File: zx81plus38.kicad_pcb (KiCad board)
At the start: 2 copper layers, 142.2 x 99.1 mm, 131 parts, among them J1 LED on, J11 Expansion Header, J12 Expansion Header, J2 KB2, J3 KB1, Q1 2N3904, Q2 2N3904, Q3 2N3904, Q4 2N3904, Q5 2N3904, Q8 2N3904, Q9 2N3904, U1 74HC541, U10 74HC86, U11 74HC08, U12 74HC32, U13 74HC00, U14 74HC393, U15 74HC11, U16 74HC32, U18 74HC74, U19 74HC32, U2 Z80CPU, U21 74HC14, U22 74HC541, U23 74HC32, U24 74HC08, U27 74HC138, U28 74HC74, U29 74HC74, U3 KM62256CLP, U4 74HC574, U5 27C256, U6 74HC125, U7 74HC393, U8 74HC4002, U9 74HC165, Y1 13MHz

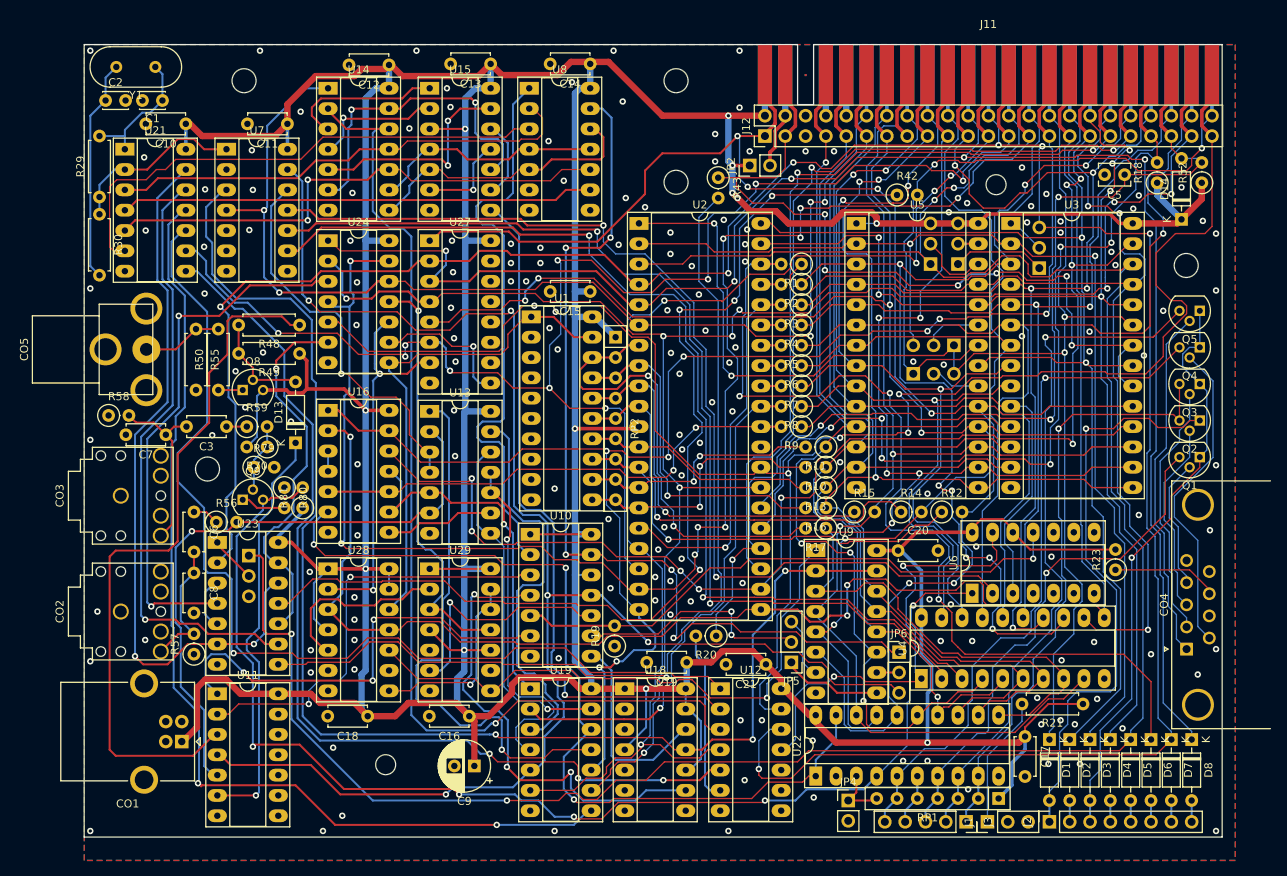
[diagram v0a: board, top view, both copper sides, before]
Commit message: fixed mounting hole positions
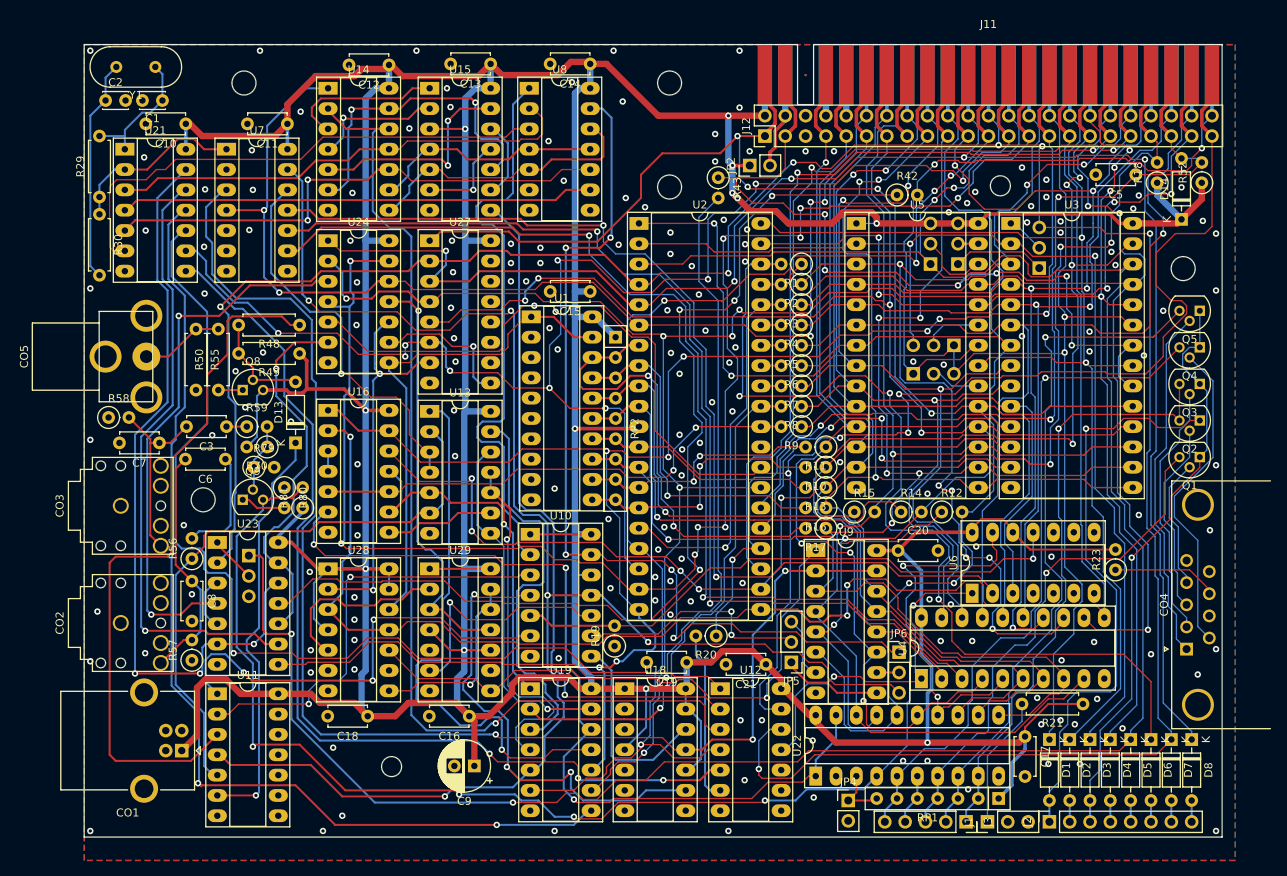
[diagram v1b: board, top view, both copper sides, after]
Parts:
- C5: footprint Capacitor_THT:C_Disc_D3.8mm_W2.6mm_P2.50mm -> Capacitor_THT:C_Disc_D4.7mm_W2.5mm_P5.00mm
- moved C6 7.69 mm to (76.1, 100.1), turned to 180 degrees
- moved R56 5.49 mm to (71.9, 112.5), turned to 90 degrees
- moved H7 3.89 mm to (73.3, 105.2)
- moved CO2 1.43 mm to (63.0, 120.6)
- moved C5 1.40 mm to (189.9, 64.5)
- moved C7 1.30 mm to (67.8, 98.0)
- moved CO3 1.26 mm to (63.0, 105.9)
- moved CO1 1.13 mm to (70.6, 136.5)
- moved C8 1.05 mm to (71.9, 115.3)
- moved H3 1.00 mm to (131.6, 66.1)
- moved CO5 0.90 mm to (61.1, 87.3)
- moved H2 0.86 mm to (131.6, 53.1)
- moved R57 0.80 mm to (71.9, 125.2)
- moved H6 0.78 mm to (96.8, 138.5)
- moved H5 0.56 mm to (172.9, 65.9)
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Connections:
- R56 pad 1: Net-(C6-Pad1) -> /nVSYNC
- R56 pad 2: /nVSYNC -> Net-(C6-Pad1)
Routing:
- net Net-(C6-Pad2): track 16.7 -> 29.9 mm
- net Net-(C6-Pad1): track 3.32 -> 14.0 mm
- net Net-(U21-Pad13): track 90.0 -> 94.0 mm, vias 2 -> 3
- net Net-(U12-Pad1): track 127.2 -> 128.7 mm
- net Net-(U23-Pad4): track 67.0 -> 68.5 mm
- net /A6': track 152.8 -> 151.5 mm
- net /nVSYNC: track 76.5 -> 75.3 mm, vias 1 -> 0
- net +5V: track 789.8 -> 791.0 mm
- net Net-(C3-Pad2): track 22.2 -> 23.2 mm
- net Net-(R48-Pad1): track 88.1 -> 89.0 mm
- net Net-(U21-Pad12): track 75.4 -> 76.2 mm
- net /nRESET: track 108.2 -> 107.5 mm
- net /A14: track 313.3 -> 312.8 mm
- net /A9: track 147.4 -> 146.9 mm
- net GND: vias 165 -> 169

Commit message: fixed keyboard connector
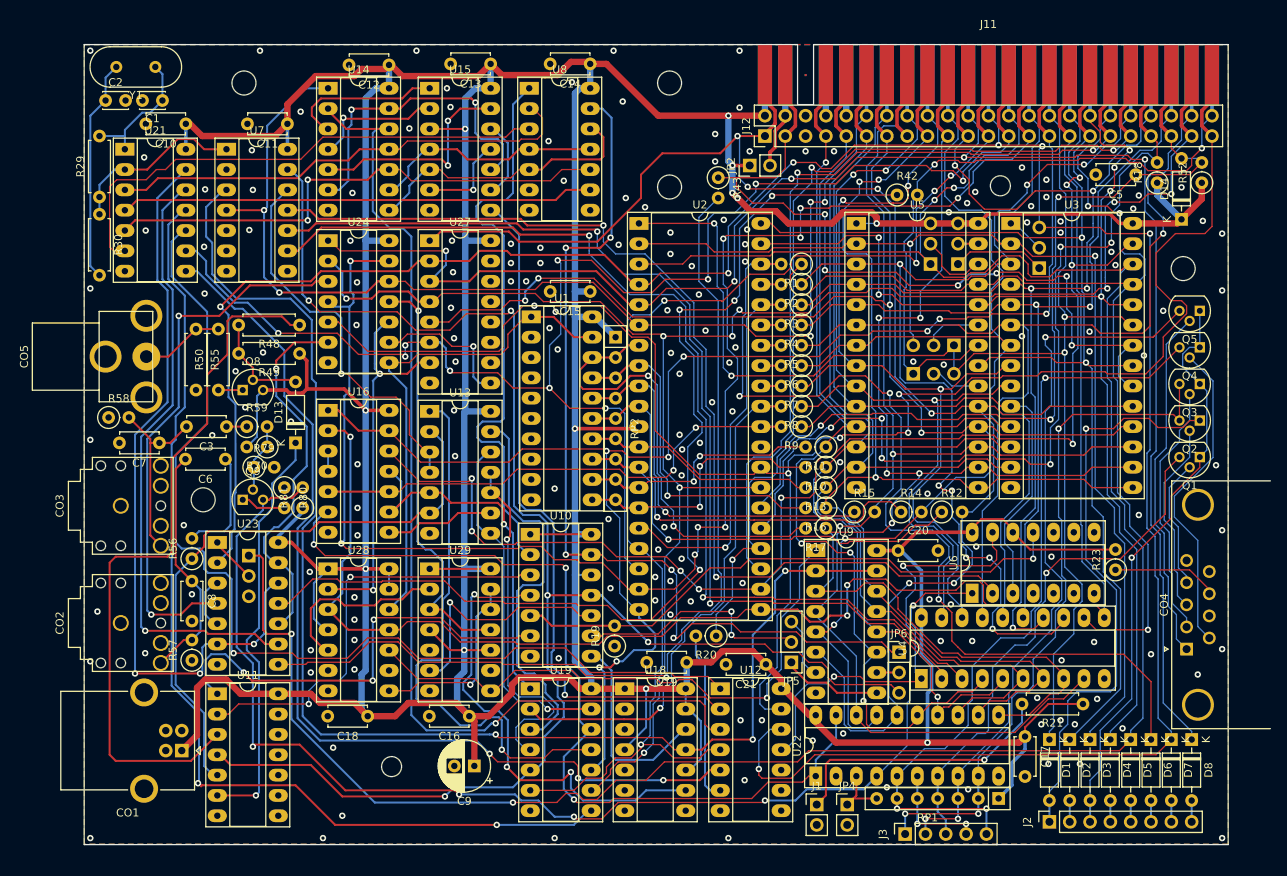
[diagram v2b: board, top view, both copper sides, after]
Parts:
- J1: footprint Connector_PinHeader_2.54mm:PinHeader_1x03_P2.54mm_Vertical -> Connector_PinHeader_2.54mm:PinHeader_1x02_P2.54mm_Vertical
- moved J1 21.4 mm to (150.0, 143.3), turned to 0 degrees
- moved J3 7.77 mm to (161.0, 146.9), turned to 90 degrees
- moved JP4 0.52 mm to (153.8, 143.3)
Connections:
- J1 pad 2: (no net) -> GND
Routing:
- net Net-(J1-Pad1): track 16.5 -> 34.5 mm, vias 0 -> 1
- net /KBD0: track 85.4 -> 97.4 mm, vias 1 -> 3
- net /KBD4: track 76.1 -> 86.1 mm, vias 1 -> 3
- net /KBD1: track 6.35 -> 13.3 mm, vias 0 -> 2
- net /KBD3: track 86.2 -> 91.2 mm, vias 1 -> 3
- net /KBD2: track 64.6 -> 65.9 mm
- net GND: vias 169 -> 168
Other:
- board size 142.2 x 99.1 mm -> 143 x 100 mm

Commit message: fixed CPU clock, memory decoder and video output latch
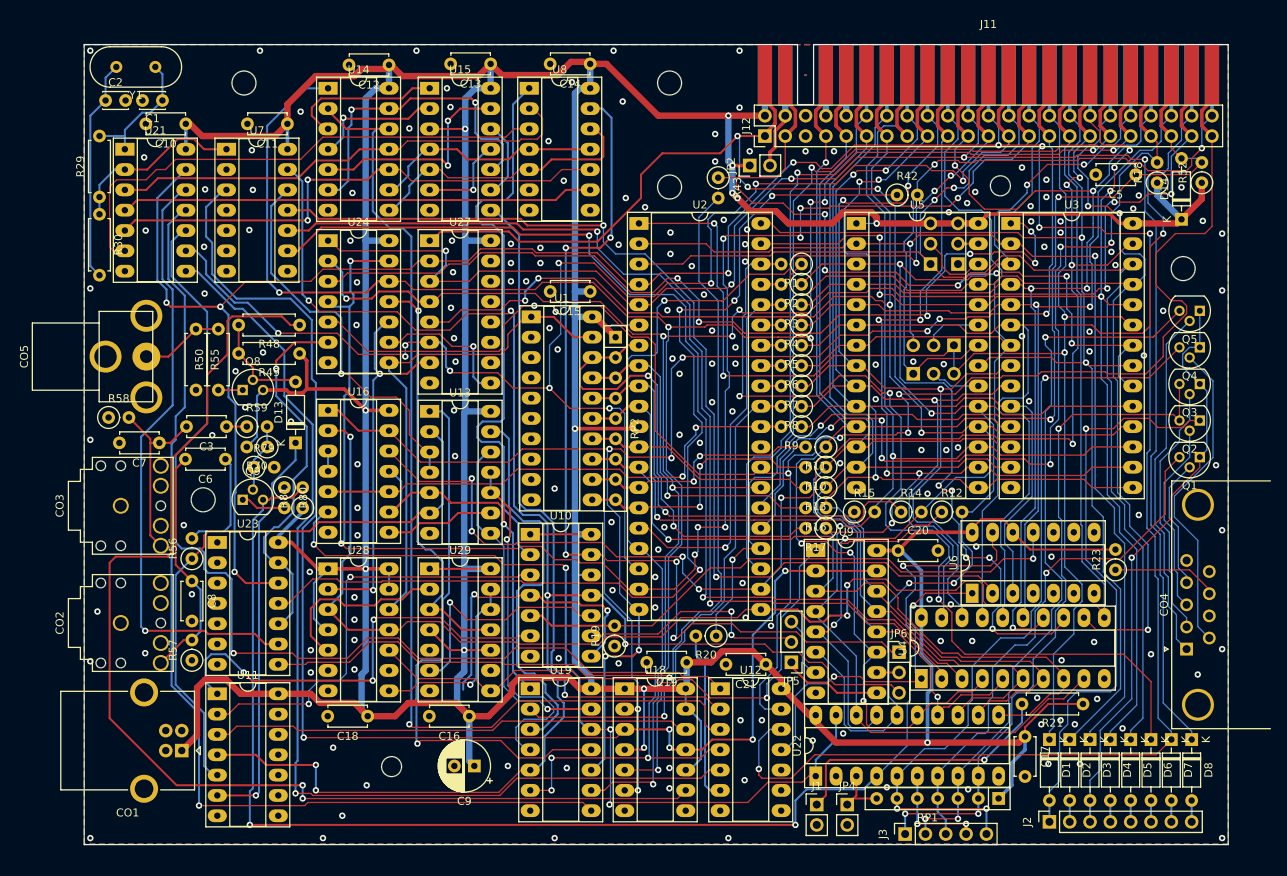
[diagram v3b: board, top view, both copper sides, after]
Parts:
- removed JP1, JP12: Jumper_3_Bridged12, Connector_PinHeader_2.54mm:PinHeader_1x03_P2.54mm_Vertical
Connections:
- U10 pad 8: Net-(U10-Pad8) -> Net-(U10-Pad4)
- U11 pad 3: Net-(R48-Pad1) -> Net-(U11-Pad3)
- U18 pad 12: Net-(U10-Pad8) -> Net-(U11-Pad3)
- U18 pad 2: GND -> /n3.25M
- U18 pad 3: GND -> /6.5M
- U18 pad 5: (no net) -> /3.25M
- U18 pad 6: (no net) -> /n3.25M
- U18 pad 9: Net-(U10-Pad4) -> Net-(R48-Pad1)
- U2 pad 6: /3.25M -> /n3.25M
- U21 pad 13: Net-(U21-Pad13) -> /A14
- U23 pad 1: Net-(JP1-Pad2) -> GND
- U23 pad 12: Net-(U21-Pad13) -> /A14
- U23 pad 2: /A14 -> GND
- U23 pad 3: Net-(U23-Pad3) -> (no net)
- U23 pad 4: Net-(U23-Pad4) -> GND
- U23 pad 5: Net-(U23-Pad3) -> GND
- U23 pad 6: Net-(U21-Pad13) -> (no net)
- U24 pad 3: Net-(U23-Pad4) -> /A14_RAM
- U3 pad 1: Net-(JP12-Pad2) -> /A14_RAM
- U7 pad 4: /3.25M -> (no net)
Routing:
- net /A13: track 301.8 -> 162.0 mm, vias 4 -> 2
- net /A14_RAM: track 0.00 -> 113.6 mm, vias 0 -> 6
- net Net-(U21-Pad13): track 94.0 -> 0.00 mm, vias 3 -> 0
- net Net-(U23-Pad4): track 68.5 -> 0.00 mm, vias 2 -> 0
- net /n3.25M: track 0.00 -> 67.4 mm, vias 0 -> 2
- net Net-(U11-Pad3): track 0.00 -> 61.0 mm
- net Net-(R48-Pad1): track 89.0 -> 146.8 mm, vias 0 -> 2
- net /3.25M: track 143.2 -> 200.5 mm, vias 5 -> 6
- net /A14: track 312.8 -> 344.8 mm, vias 7 -> 10
- net Net-(U10-Pad8): track 25.0 -> 0.00 mm
- net Net-(U10-Pad4): track 59.5 -> 36.8 mm, vias 3 -> 2
- net GND: track 21.8 -> 10.8 mm, vias 168 -> 178
- net Net-(U23-Pad3): track 6.79 -> 0.00 mm
- net /nCAS_IN: track 167.8 -> 174.6 mm, vias 5 -> 3
- net Net-(U12-Pad5): track 122.1 -> 128.7 mm, vias 3 -> 1
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
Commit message: finished rev 2.0
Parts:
- removed JP10: Jumper_3_Bridged12, Connector_PinHeader_2.54mm:PinHeader_1x03_P2.54mm_Vertical
- CO1: footprint Connector_USB:USB_B_OST_USB-B1HSxx_Horizontal -> modusoft:Jack_Barrel_CLIFF_FCR681465P
- moved CO1 6.74 mm to (64.0, 135.3), turned to 90 degrees
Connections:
- CO1 pad 2: (no net) -> GND
- JP11 pad 2: Net-(JP11-Pad2) -> /nROMCS
- JP8 pad 2: Net-(JP8-Pad2) -> /A11
- JP9 pad 2: Net-(JP9-Pad2) -> /A13
- U5 pad 20: Net-(JP11-Pad2) -> /nROMCS
- U5 pad 23: Net-(JP8-Pad2) -> /A11
- U5 pad 26: Net-(JP9-Pad2) -> /A13
- U5 pad 27: Net-(JP10-Pad2) -> /A15
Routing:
- net Net-(U10-Pad4): track 36.8 -> 16.7 mm, vias 2 -> 1
- net /A15: track 210.6 -> 225.7 mm, vias 5 -> 6
- net /A11: track 173.9 -> 183.9 mm
- net /A13: track 162.0 -> 171.1 mm
- net Net-(JP9-Pad2): track 8.89 -> 0.00 mm
- net /nROMCS: track 85.0 -> 93.7 mm
- net Net-(JP8-Pad2): track 7.38 -> 0.00 mm
- net Net-(R48-Pad1): track 146.8 -> 153.1 mm
- net Net-(JP11-Pad2): track 6.22 -> 0.00 mm
- net Net-(JP10-Pad2): track 2.54 -> 0.00 mm
- net +5V: track 792.3 -> 791.1 mm
- net /A3': track 105.1 -> 106.1 mm, vias 0 -> 2
- net /A6': track 151.5 -> 152.5 mm
- net /A0': track 101.1 -> 101.7 mm
- net GND: vias 178 -> 189
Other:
- board text added: "07/01/2022"
- board text added: "Rev 2.0"
- board text added: "ZX81#"
